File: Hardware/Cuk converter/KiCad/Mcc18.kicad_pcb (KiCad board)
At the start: 2 copper layers, 47 parts, among them Q1 IRFP4321PbF, U1 LTSP_25-NP, U2 DRIVER_(INEP), U3 LM7812_TO220, U4 Signals_MCC, U5 ZCS

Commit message: snubber update
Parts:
- moved Ds2 27.3 mm to (179.4, 59.4)
- moved Rs3 9.91 mm to (192.8, 60.7)
- moved Rs2 8.28 mm to (221.5, 65.5)
- moved Ds1 3.09 mm to (209.6, 58.9)
- moved Cs1 1.83 mm to (203.5, 52.6)
- moved Cs2 1.80 mm to (200.2, 52.8)
- moved Rs1 1.63 mm to (210.8, 53.1)
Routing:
- net /+Vp: track 307.6 -> 285.7 mm, vias 5 -> 3
- net Net-(Cs2-Pad1): track 14.7 -> 0.00 mm
- net /Source: track 143.1 -> 131.9 mm, vias 1 -> 2
- net Net-(Cs3-Pad1): track 13.9 -> 9.09 mm
- net Net-(Cs1-Pad1): track 2.23 -> 0.58 mm
- net GNDA: vias 14 -> 15

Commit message: Snubber finished
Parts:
- Ds2, Rs2: moved to B.Cu
- moved Ds2 30.1 mm to (209.5, 61.7)
- moved Rs2 13.1 mm to (212.3, 56.1), turned to 0 degrees
- moved Rs3 5.09 mm to (197.9, 61.0)
- moved Cs4 3.53 mm to (202.2, 67.6), turned to 270 degrees
- moved Rs4 3.41 mm to (209.6, 68.1)
- moved Cs3 0.91 mm to (197.9, 67.6)
- moved Cs1 0.26 mm to (203.5, 52.8)
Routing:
- net /+Vp: track 285.7 -> 314.2 mm
- net /-B: track 273.7 -> 293.2 mm, vias 3 -> 4
- net Net-(Cs2-Pad1): track 0.00 -> 14.6 mm, vias 0 -> 1
- net /Source: track 131.9 -> 143.5 mm
- net /-Vp: track 347.1 -> 336.0 mm
- net Net-(Cs3-Pad1): track 9.09 -> 18.1 mm, vias 0 -> 1
- net Net-(Cs1-Pad1): track 0.58 -> 4.87 mm
- net Net-(Cs4-Pad1): track 2.53 -> 5.19 mm

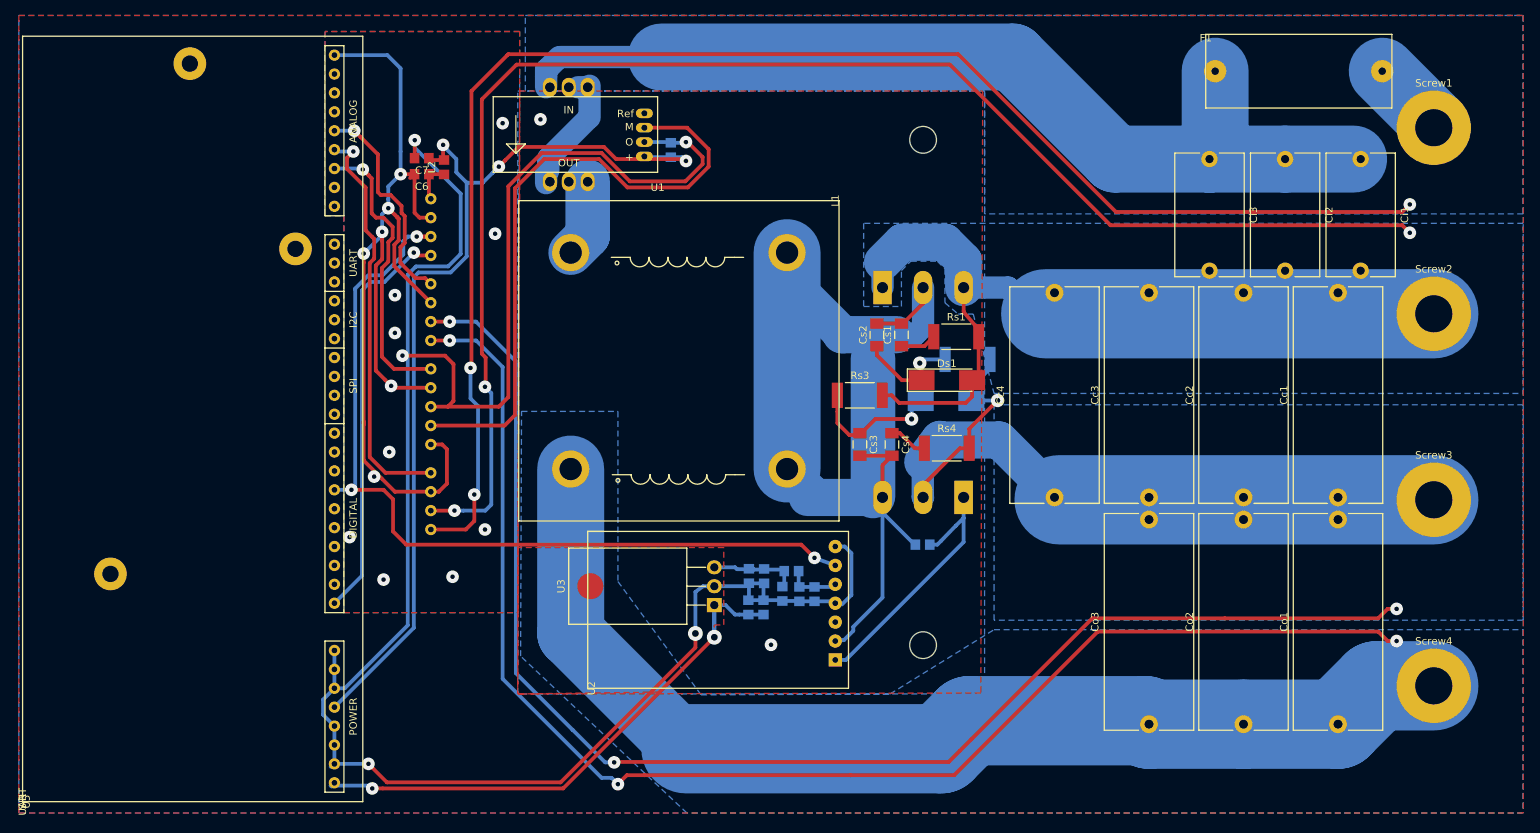
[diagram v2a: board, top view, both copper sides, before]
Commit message: Add cut board layer
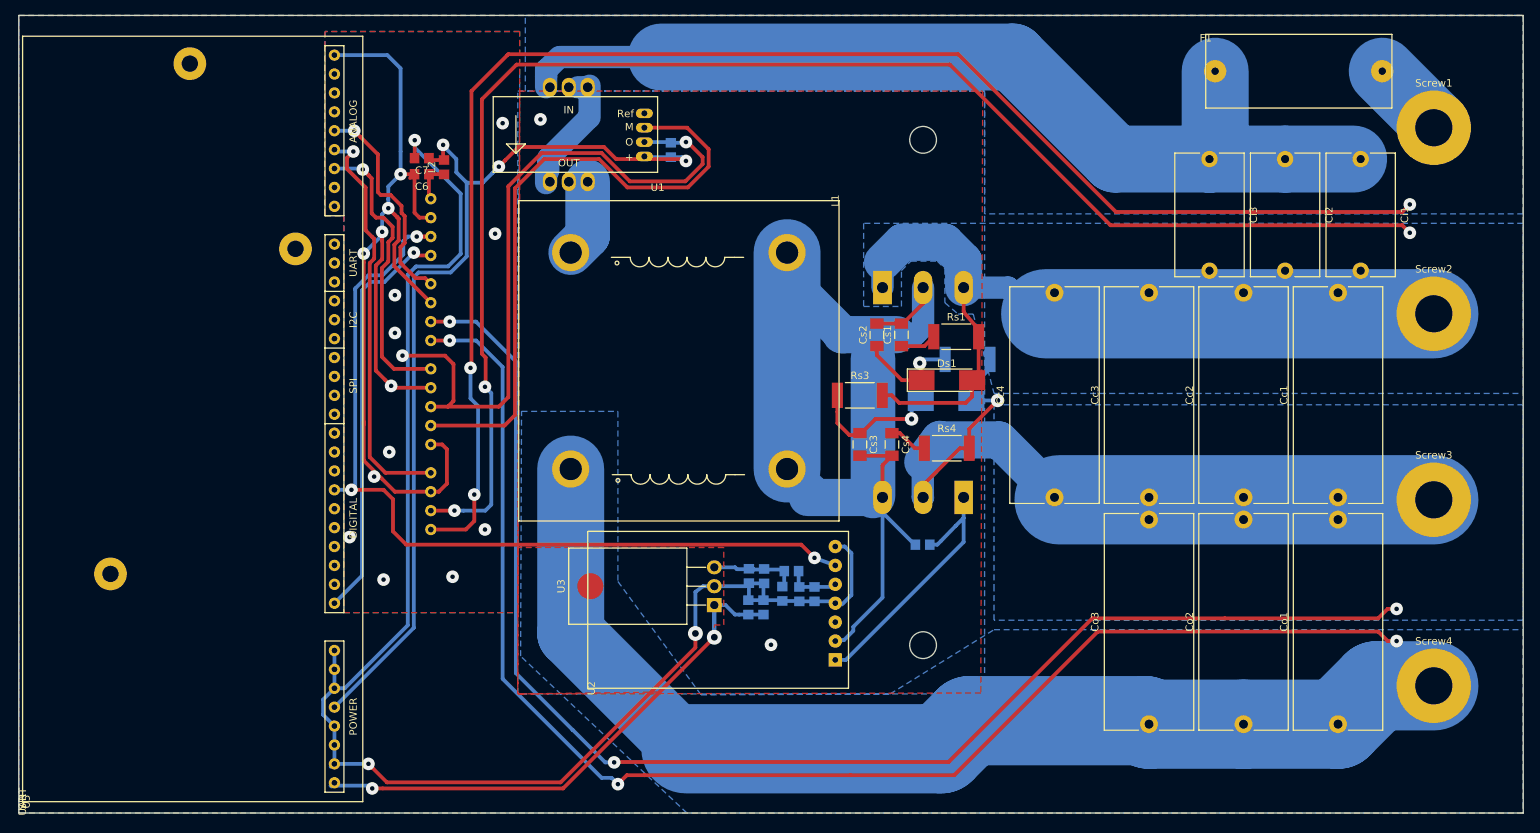
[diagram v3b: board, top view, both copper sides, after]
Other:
- board outline added: 202.2 x 107.2 mm
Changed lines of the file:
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@@
   (general
     (thickness 1.6)
-    (drawings 0)
+    (drawings 9)
     (tracks 515)
     (zones 0)
@@
   )
   (setup
-    (last_trace_width 9)
+    (last_trace_width 0.508)
     (user_trace_width 0.508)
     (user_trace_width 3)
@@
     )
   )
+  (target plus (at 84.836 9.906) (size 5) (width 0.15) (layer Edge.Cuts))
+  (gr_line (start 84.836 117.094) (end 84.836 9.906) (layer Edge.Cuts) (width 0.15))
+  (gr_line (start 287.02 117.094) (end 84.836 117.094) (layer Edge.Cuts) (width 0.15))
+  (gr_line (start 287.02 9.906) (end 287.02 117.094) (layer Edge.Cuts) (width 0.15))
+  (gr_line (start 84.836 9.906) (end 287.02 9.906) (layer Edge.Cuts) (width 0.15))
+  (dimension 202.184 (width 0.3) (layer Dwgs.User)
+    (gr_text "7.9600 in" (at 185.928 125.29) (layer Dwgs.User)
+      (effects (font (size 1.5 1.5) (thickness 0.3)))
+    )
+    (feature1 (pts (xy 287.02 117.094) (xy 287.02 123.776421)))
+    (feature2 (pts (xy 84.836 117.094) (xy 84.836 123.776421)))
+    (crossbar (pts (xy 84.836 123.19) (xy 287.02 123.19)))
+    (arrow1a (pts (xy 287.02 123.19) (xy 285.893496 123.776421)))
+    (arrow1b (pts (xy 287.02 123.19) (xy 285.893496 122.603579)))
+    (arrow2a (pts (xy 84.836 123.19) (xy 85.962504 123.776421)))
+    (arrow2b (pts (xy 84.836 123.19) (xy 85.962504 122.603579)))
+  )
+  (dimension 202.18416 (width 0.3) (layer Dwgs.User)
+    (gr_text "202.184 mm" (at 185.946273 131.766339 0.07197958464) (layer Dwgs.User)
+      (effects (font (size 1.5 1.5) (thickness 0.3)))
+    )
+    (feature1 (pts (xy 84.836 117.348) (xy 84.852372 130.379761)))
+    (feature2 (pts (xy 287.02 117.094) (xy 287.036372 130.125761)))
+    (crossbar (pts (xy 287.035635 129.539341) (xy 84.851635 129.793341)))
+    (arrow1a (pts (xy 84.851635 129.793341) (xy 85.977401 129.205506)))
+    (arrow1b (pts (xy 84.851635 129.793341) (xy 85.978875 130.378346)))
+    (arrow2a (pts (xy 287.035635 129.539341) (xy 285.908395 128.954336)))
+    (arrow2b (pts (xy 287.035635 129.539341) (xy 285.909869 130.127176)))
+  )
+  (dimension 107.188301 (width 0.3) (layer Dwgs.User)
+    (gr_text "4.2200 in" (at 76.009258 63.521217 270.1357717) (layer Dwgs.User)
+      (effects (font (size 1.5 1.5) (thickness 0.3)))
+    )
+    (feature1 (pts (xy 85.09 117.094) (xy 77.649833 117.111631)))
+    (feature2 (pts (xy 84.836 9.906) (xy 77.395833 9.923631)))
+    (crossbar (pts (xy 77.982252 9.922241) (xy 78.236252 117.110241)))
+    (arrow1a (pts (xy 78.236252 117.110241) (xy 77.647163 115.98513)))
+    (arrow1b (pts (xy 78.236252 117.110241) (xy 78.820002 115.982351)))
+    (arrow2a (pts (xy 77.982252 9.922241) (xy 77.398502 11.050131)))
+    (arrow2b (pts (xy 77.982252 9.922241) (xy 78.571341 11.047352)))
+  )
+  (dimension 107.188 (width 0.3) (layer Dwgs.User)
+    (gr_text "107.188 mm" (at 71.306 63.5 270) (layer Dwgs.User)
+      (effects (font (size 1.5 1.5) (thickness 0.3)))
+    )
+    (feature1 (pts (xy 84.836 117.094) (xy 72.819579 117.094)))
+    (feature2 (pts (xy 84.836 9.906) (xy 72.819579 9.906)))
+    (crossbar (pts (xy 73.406 9.906) (xy 73.406 117.094)))
+    (arrow1a (pts (xy 73.406 117.094) (xy 72.819579 115.967496)))
+    (arrow1b (pts (xy 73.406 117.094) (xy 73.992421 115.967496)))
+    (arrow2a (pts (xy 73.406 9.906) (xy 72.819579 11.032504)))
+    (arrow2b (pts (xy 73.406 9.906) (xy 73.992421 11.032504)))
+  )
   (segment (start 275 24.3274) (end 268.0716 17.399) (width 9) (layer B.Cu) (net 36))

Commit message: add a fill zone witout net
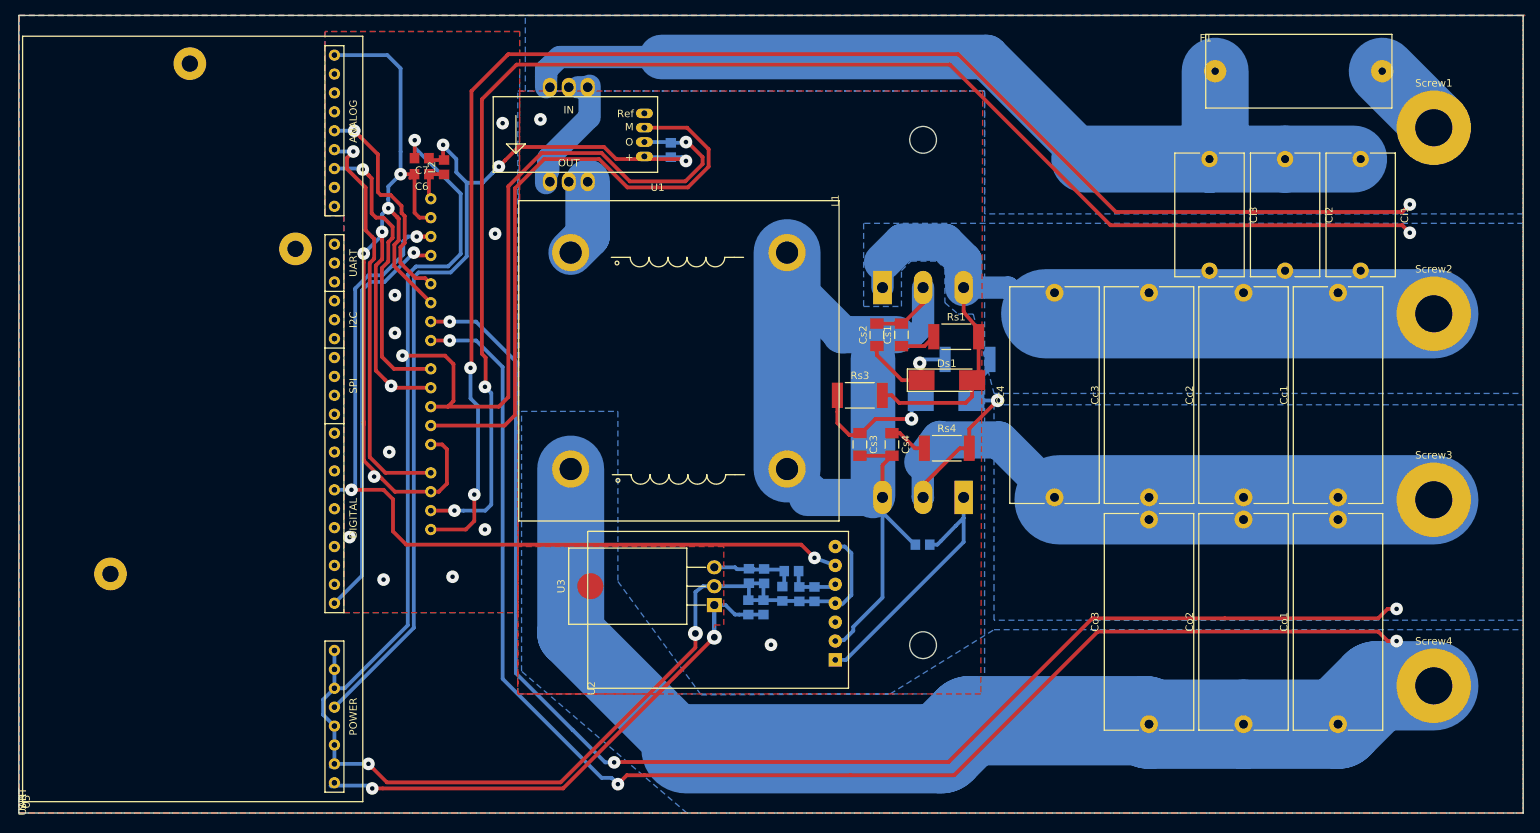
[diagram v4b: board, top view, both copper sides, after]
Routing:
- added copper zone on B.Cu, net (none)
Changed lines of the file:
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@@
     (thickness 1.6)
     (drawings 9)
-    (tracks 515)
+    (tracks 516)
     (zones 0)
     (modules 47)
@@
   )
   (setup
-    (last_trace_width 0.508)
+    (last_trace_width 6)
     (user_trace_width 0.508)
     (user_trace_width 3)
@@
     (user_trace_width 12)
     (trace_clearance 0.3048)
-    (zone_clearance 1.27)
+    (zone_clearance 0.3048)
     (zone_45_only no)
     (trace_min 0.508)
@@
   (segment (start 151.511 63.627) (end 150.114 65.024) (width 0.508) (layer F.Cu) (net 49))
   (segment (start 150.114 65.024) (end 140.208 65.024) (width 0.508) (layer F.Cu) (net 49))
-  (segment (start 244.856 29.21) (end 232.156 29.21) (width 9) (layer B.Cu) (net 50))
-  (segment (start 232.156 29.21) (end 218.44 15.494) (width 9) (layer B.Cu) (net 50))
-  (segment (start 218.44 15.494) (end 171.196 15.494) (width 9) (layer B.Cu) (net 50))
   (segment (start 171.196 15.494) (end 157.734 15.494) (width 3) (layer B.Cu) (net 50))
   (segment (start 155.702 18.096921) (end 155.702 19.558) (width 3) (layer B.Cu) (net 50))
@@
   (segment (start 145.542 57.277) (end 145.542 61.386532) (width 0.508) (layer B.Cu) (net 50))
   (segment (start 146.557979 73.787021) (end 146.05 74.295) (width 0.508) (layer B.Cu) (net 50))
+  (segment (start 244.856 29.21) (end 228.092 29.21) (width 9) (layer B.Cu) (net 50))
+  (segment (start 228.092 29.21) (end 228.092 28.702) (width 6) (layer B.Cu) (net 50))
+  (segment (start 214.884 15.494) (end 171.196 15.494) (width 6) (layer B.Cu) (net 50))
+  (segment (start 228.092 28.702) (end 214.884 15.494) (width 6) (layer B.Cu) (net 50))
   (zone (net 41) (net_name GND) (layer F.Cu) (hatch edge 0.508)
     (connect_pads yes (clearance 0.3048))
@@
     (polygon
       (pts
-        (xy 214.63 20.066) (xy 214.63 101.092) (xy 154.432 101.092) (xy 152.4 101.092) (xy 151.892 101.092)
+        (xy 214.63 20.066) (xy 214.63 101.092) (xy 151.892 101.092) (xy 152.4 101.092) (xy 151.892 101.092)
         (xy 151.892 20.066)
       )
@@
     (polygon
       (pts
-        (xy 214.376 20.066) (xy 214.122 100.965) (xy 154.432 101.092) (xy 152.4 101.092) (xy 151.892 101.092)
-        (xy 152.146 20.066)
+        (xy 214.376 20.066) (xy 214.122 101.092) (xy 151.892 101.092) (xy 152.146 20.066)
       )
     )
@@
     (polygon
       (pts
-        (xy 287.02 92.456) (xy 287.02 117.094) (xy 174.625 117.094) (xy 152.273 96.012) (xy 152.4 63.119)
+        (xy 287.02 92.456) (xy 287.02 117.094) (xy 174.625 117.094) (xy 152.4 98.044) (xy 152.4 63.119)
         (xy 165.354 63.119) (xy 165.354 85.979) (xy 176.53 101.219) (xy 201.93 101.092) (xy 215.9 92.456)
       )
@@
     )
   )
-  (zone (net 0) (net_name "") (layer F.Cu) (hatch edge 0.508)
+  (zone (net 41) (net_name GND) (layer F.Cu) (hatch edge 0.508)
     (priority 6)
     (connect_pads yes (clearance 0.3048))
@@
     (polygon
       (pts
-        (xy 179.578 81.407) (xy 151.892 81.407) (xy 151.892 101.092) (xy 170.942 100.838) (xy 178.308 93.472)
+        (xy 179.578 81.28) (xy 151.892 81.28) (xy 151.892 101.092) (xy 170.942 101.092) (xy 178.308 93.472)
         (xy 178.308 91.948) (xy 178.308 91.821) (xy 179.578 91.821)
       )
@@
       )
     )
+  )
+  (zone (net 0) (net_name "") (layer B.Cu) (hatch edge 0.508)
+    (connect_pads no (clearance 0.3048))
+    (min_thickness 0.508)
+    (fill yes (arc_segments 16) (thermal_gap 0.508) (thermal_bridge_width 0.5334))
+    (polygon
+      (pts
+        (xy 84.836 9.906) (xy 84.836 117.094) (xy 287.02 117.094) (xy 287.02 9.906) (xy 287.274 9.906)
+        (xy 287.02 9.906)
+      )
+    )
+  )
+  (zone (net 0) (net_name "") (layer F.Cu) (hatch edge 0.508)
+    (connect_pads no (clearance 0.3048))
+    (min_thickness 0.508)
+    (fill yes (arc_segments 16) (thermal_gap 0.508) (thermal_bridge_width 0.5334))
+    (polygon
+      (pts
+        (xy 84.836 9.906) (xy 84.836 117.094) (xy 287.02 117.094) (xy 287.02 9.906) (xy 287.274 9.906)
+        (xy 287.02 9.906)
+      )
+    )

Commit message: Fixed errors
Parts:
- moved Rs3 2.09 mm to (199.9, 60.5)
- moved Ds1 1.80 mm to (211.3, 58.7)
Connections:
- U5 pad 31: /Ipanel_adc+ -> /Vpanel_adc+
- U5 pad 32: /Vpanel_adc+ -> /Ipanel_adc+
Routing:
- net GND: track 301.6 -> 379.1 mm, vias 5 -> 7
- net /+B: track 336.5 -> 292.6 mm
- net /-Vp: track 336.3 -> 296.9 mm
- net /+Vp: track 314.2 -> 275.1 mm
- net /-B: track 293.2 -> 255.7 mm
- net /Vpanel_adc+: track 54.9 -> 48.1 mm
- net +5V: track 128.7 -> 132.3 mm
- net Net-(Cs3-Pad1): track 18.1 -> 15.6 mm
- net /Ipanel_adc+: track 40.3 -> 42.3 mm
- net /PWM: track 116.2 -> 115.0 mm
- net Net-(Cs2-Pad1): track 14.6 -> 15.5 mm
- net /Vbat_adc+: track 29.5 -> 30.3 mm
- removed copper zone on B.Cu, net (none)
- removed copper zone on F.Cu, net (none)
